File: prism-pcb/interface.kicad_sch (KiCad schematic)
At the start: 8 parts, among them J301 FFC_P1mm_BOT_RA_SMD, U301 TPSM365R6V5RDNR

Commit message: tmc5130-uart -> prism-pcb
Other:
- title: tmc5130-uart -> prism-pcb
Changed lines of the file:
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@@
   (paper "A4")
   (title_block
-    (title "tmc5130-uart")
+    (title "prism-pcb")
     (date "2024-07-11")
     (rev "1.0")
@@
     (pin "2")
     (instances
-      (project "tmc5130-uart"
+      (project "prism-pcb"
         (path "/df2b2e89-e055-4140-95de-f1df723db034/c1dd8f61-494c-402f-8e59-08309c64fc3f"
           (reference "R301") (unit 1)
@@
     (pin "1")
     (instances
-      (project "tmc5130-uart"
+      (project "prism-pcb"
         (path "/df2b2e89-e055-4140-95de-f1df723db034/c1dd8f61-494c-402f-8e59-08309c64fc3f"
           (reference "R302") (unit 1)
@@
     (pin "1")
     (instances
-      (project "tmc5130-uart"
+      (project "prism-pcb"
         (path "/df2b2e89-e055-4140-95de-f1df723db034/c1dd8f61-494c-402f-8e59-08309c64fc3f"
           (reference "#FLG0303") (unit 1)
@@
     (pin "1")
     (instances
-      (project "tmc5130-uart"
+      (project "prism-pcb"
         (path "/df2b2e89-e055-4140-95de-f1df723db034/c1dd8f61-494c-402f-8e59-08309c64fc3f"
           (reference "C304") (unit 1)
@@
     (pin "4")
     (instances
-      (project "tmc5130-uart"
+      (project "prism-pcb"
         (path "/df2b2e89-e055-4140-95de-f1df723db034/c1dd8f61-494c-402f-8e59-08309c64fc3f"
           (reference "U301") (unit 1)
@@
     (pin "2")
     (instances
-      (project "tmc5130-uart"
+      (project "prism-pcb"
         (path "/df2b2e89-e055-4140-95de-f1df723db034/c1dd8f61-494c-402f-8e59-08309c64fc3f"
           (reference "C301") (unit 1)
@@
     (pin "1")
     (instances
-      (project "tmc5130-uart"
+      (project "prism-pcb"
         (path "/df2b2e89-e055-4140-95de-f1df723db034/c1dd8f61-494c-402f-8e59-08309c64fc3f"
           (reference "C303") (unit 1)
@@
     (pin "7")
     (instances
-      (project "tmc5130-uart"
+      (project "prism-pcb"
         (path "/df2b2e89-e055-4140-95de-f1df723db034/c1dd8f61-494c-402f-8e59-08309c64fc3f"
           (reference "J301") (unit 1)
@@
     (pin "1")
     (instances
-      (project "tmc5130-uart"
+      (project "prism-pcb"
         (path "/df2b2e89-e055-4140-95de-f1df723db034/c1dd8f61-494c-402f-8e59-08309c64fc3f"
           (reference "#FLG0302") (unit 1)
@@
     (pin "1")
     (instances
-      (project "tmc5130-uart"
+      (project "prism-pcb"
         (path "/df2b2e89-e055-4140-95de-f1df723db034/c1dd8f61-494c-402f-8e59-08309c64fc3f"
           (reference "#FLG0301") (unit 1)
@@
     (pin "2")
     (instances
-      (project "tmc5130-uart"
+      (project "prism-pcb"
         (path "/df2b2e89-e055-4140-95de-f1df723db034/c1dd8f61-494c-402f-8e59-08309c64fc3f"
           (reference "C302") (unit 1)

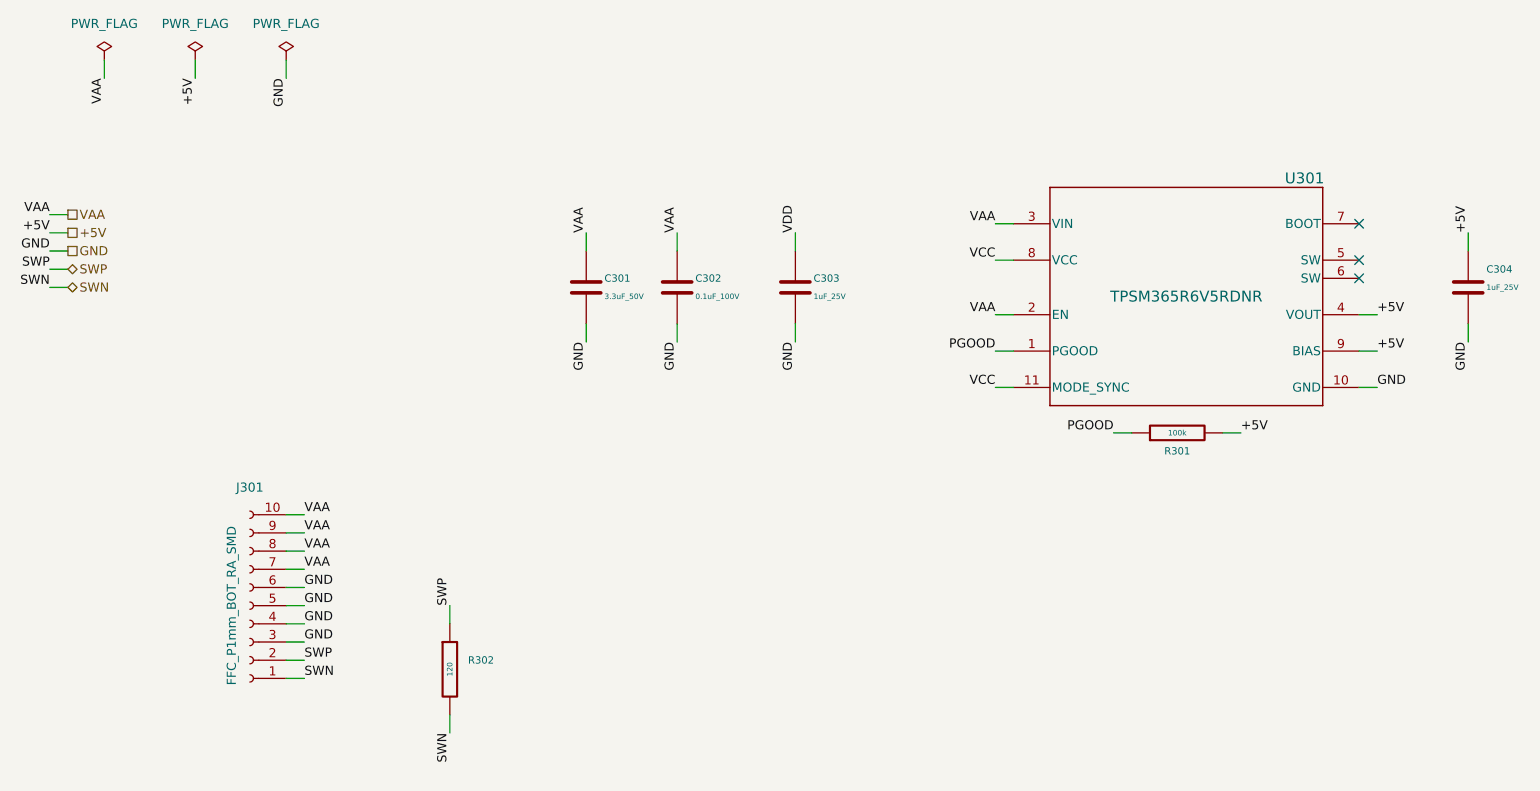
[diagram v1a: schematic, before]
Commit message: Update power supply connections
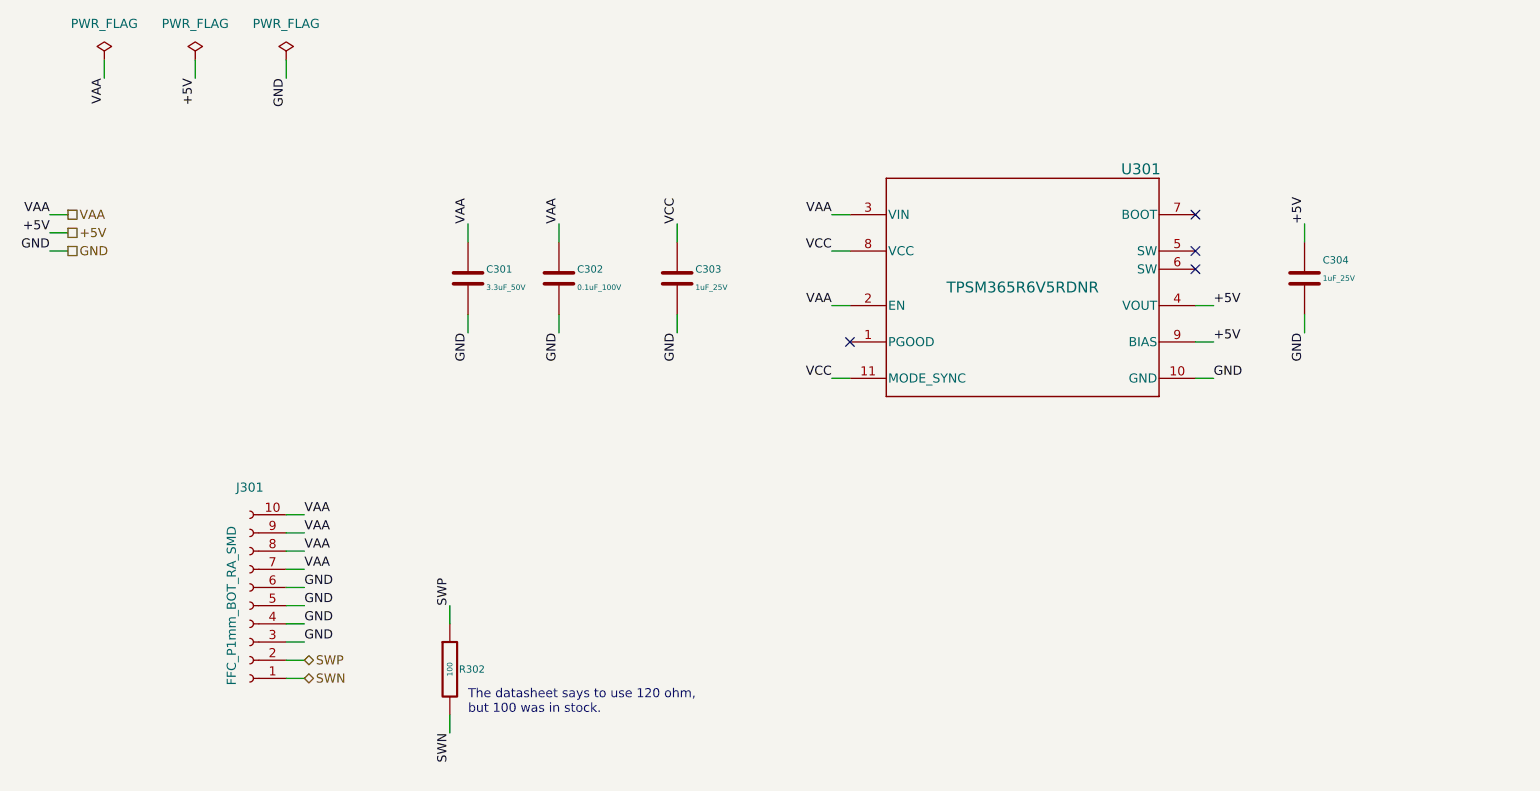
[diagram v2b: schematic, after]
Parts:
- removed R301: 100k, Janelia:R_0402_1005Metric, symbol Janelia:R_100k_0402
- removed R302: 120, Janelia:R_0402_1005Metric, symbol Janelia:R_120_0402
- added R302: 100, Janelia:R_0402_1005Metric, symbol Janelia:R_100_0402
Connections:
- net VDD is gone; now on net VCC: C303.1
- net SWN: now also R302.2
- net SWP: now also R302.1
- net PGOOD: no longer names the net of U301.1 (PGOOD)
- no-connect marks 3 -> 4
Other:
- note added: "The datasheet says to use 120 ohm, but 100 was in stock."
- moved on the sheet: C301, C302, C303, C304, U301

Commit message: Initial footprint layout
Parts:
- renumbered R302 to R301
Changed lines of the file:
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@@
   (symbol (lib_id "Janelia:R_100_0402") (at 113.03 121.92 0) (unit 1)
     (in_bom yes) (on_board yes) (dnp no)
-    (property "Reference" "R302" (at 114.3 121.92 0)
+    (property "Reference" "R301" (at 114.3 121.92 0)
       (effects (font (size 1.016 1.016)) (justify left))
     )
@@
       (project "prism-pcb"
         (path "/df2b2e89-e055-4140-95de-f1df723db034/c1dd8f61-494c-402f-8e59-08309c64fc3f"
-          (reference "R302") (unit 1)
+          (reference "R301") (unit 1)
         )
       )

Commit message: Place all footprints
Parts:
- added M301: Fan_5VDC_25x25x8mm, Janelia:FAN_5VDC_25x25x8mm, symbol Janelia:Fan_5VDC_25x25x8mm
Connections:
- net +5V: now also M301.1 (+5V)
- net GND: now also M301.2 (GND), M301.3 (MH)
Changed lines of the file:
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@@
+    (stroke (width 0) (type default))
+  )
+  (wire (pts (xy 186.69 129.54) (xy 186.69 132.08))
     (stroke (width 0) (type default))
   )
@@
   )
   (wire (pts (xy 90.17 123.19) (xy 92.71 123.19))
+    (stroke (width 0) (type default))
+  )
+  (wire (pts (xy 186.69 111.76) (xy 186.69 109.22))
     (stroke (width 0) (type default))
   )
@@
     (effects (font (size 1.27 1.27)) (justify left bottom))
   )
+  (label "GND" (at 186.69 132.08 270) (fields_autoplaced)
+    (effects (font (size 1.27 1.27)) (justify right bottom))
+  )
   (label "VAA" (at 92.71 105.41 0) (fields_autoplaced)
     (effects (font (size 1.27 1.27)) (justify left bottom))
@@
   )
   (label "GND" (at 92.71 115.57 0) (fields_autoplaced)
+    (effects (font (size 1.27 1.27)) (justify left bottom))
+  )
+  (label "+5V" (at 186.69 109.22 90) (fields_autoplaced)
     (effects (font (size 1.27 1.27)) (justify left bottom))
   )
@@
         )
       )
+    )
+  )
+  (symbol (lib_id "Janelia:Fan_5VDC_25x25x8mm") (at 186.69 120.65 0) (unit 1)
+    (in_bom no) (on_board yes) (dnp no) (fields_autoplaced)
+    (property "Reference" "M301" (at 190.5 120.65 0) (do_not_autoplace)
+      (effects (font (size 1.27 1.27)) (justify left))
+    )
+    (property "Value" "Fan_5VDC_25x25x8mm" (at 186.69 115.57 0) (do_not_autoplace)
+      (effects (font (size 1.27 1.27)) (justify top) hide)
+    )
+    (property "Footprint" "Janelia:FAN_5VDC_25x25x8mm" (at 186.69 102.87 0)
+      (effects (font (size 1.27 1.27)) hide)
+    )
+    (property "Datasheet" "~" (at 186.69 104.14 0)
+      (effects (font (size 1.27 1.27)) hide)
+    )
+    (property "Synopsis" "FAN AXIAL 25X8MM 5VDC WIRE" (at 186.69 114.3 0)
+      (effects (font (size 1.27 1.27)) hide)
+    )
+    (property "Manufacturer" "ebm-papst Inc." (at 186.69 111.76 0)
+      (effects (font (size 1.27 1.27)) hide)
+    )
+    (property "Manufacturer Part Number" "255M" (at 186.69 113.03 0) (do_not_autoplace)
+      (effects (font (size 1.27 1.27)) hide)
+    )
+    (property "Vendor" "Digi-Key" (at 186.69 109.22 0)
+      (effects (font (size 1.27 1.27)) hide)
+    )
+    (property "Vendor Part Number" "381-2353-ND" (at 186.69 106.68 0)
+      (effects (font (size 1.27 1.27)) hide)
+    )
+    (property "LCSC" "" (at 186.69 120.65 0)
+      (effects (font (size 1.27 1.27)) hide)
+    )
+    (property "Sim.Enable" "0" (at 186.69 120.65 0)
+      (effects (font (size 1.27 1.27)) hide)
+    )
+    (pin "3")
+    (pin "1")
+    (pin "2")
+    (instances
+      (project "prism-pcb"
+        (path "/df2b2e89-e055-4140-95de-f1df723db034/c1dd8f61-494c-402f-8e59-08309c64fc3f"
+          (reference "M301") (unit 1)
+        )
+      )
